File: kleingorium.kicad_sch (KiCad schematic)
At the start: 35 parts, among them J1 4017 Pins, J10 VCC, J11 GND, J12 4046 Comp In, J13 Select, J14 Input, J15 4046 SigIn, J16 4046 Comp, J17 Output, J18 4046 Comp In, J19 4046 Out, J2 4040 Output, J20 4040 Input, J21 4040 Output, J22 4017 Pins, J23 VCC, J24 GND, J3 4040 Input, J4 4046 Out, J5 4046 Comp, J6 Select, J7 Output, J8 Input, J9 4046 SigIn, Q1 2N3904, Q2 2N3904, SW1 4017 Feedback, SW2 4046 CompIn, SW3 Chain, SW4 4017 Feedback, SW5 4046 CompIn

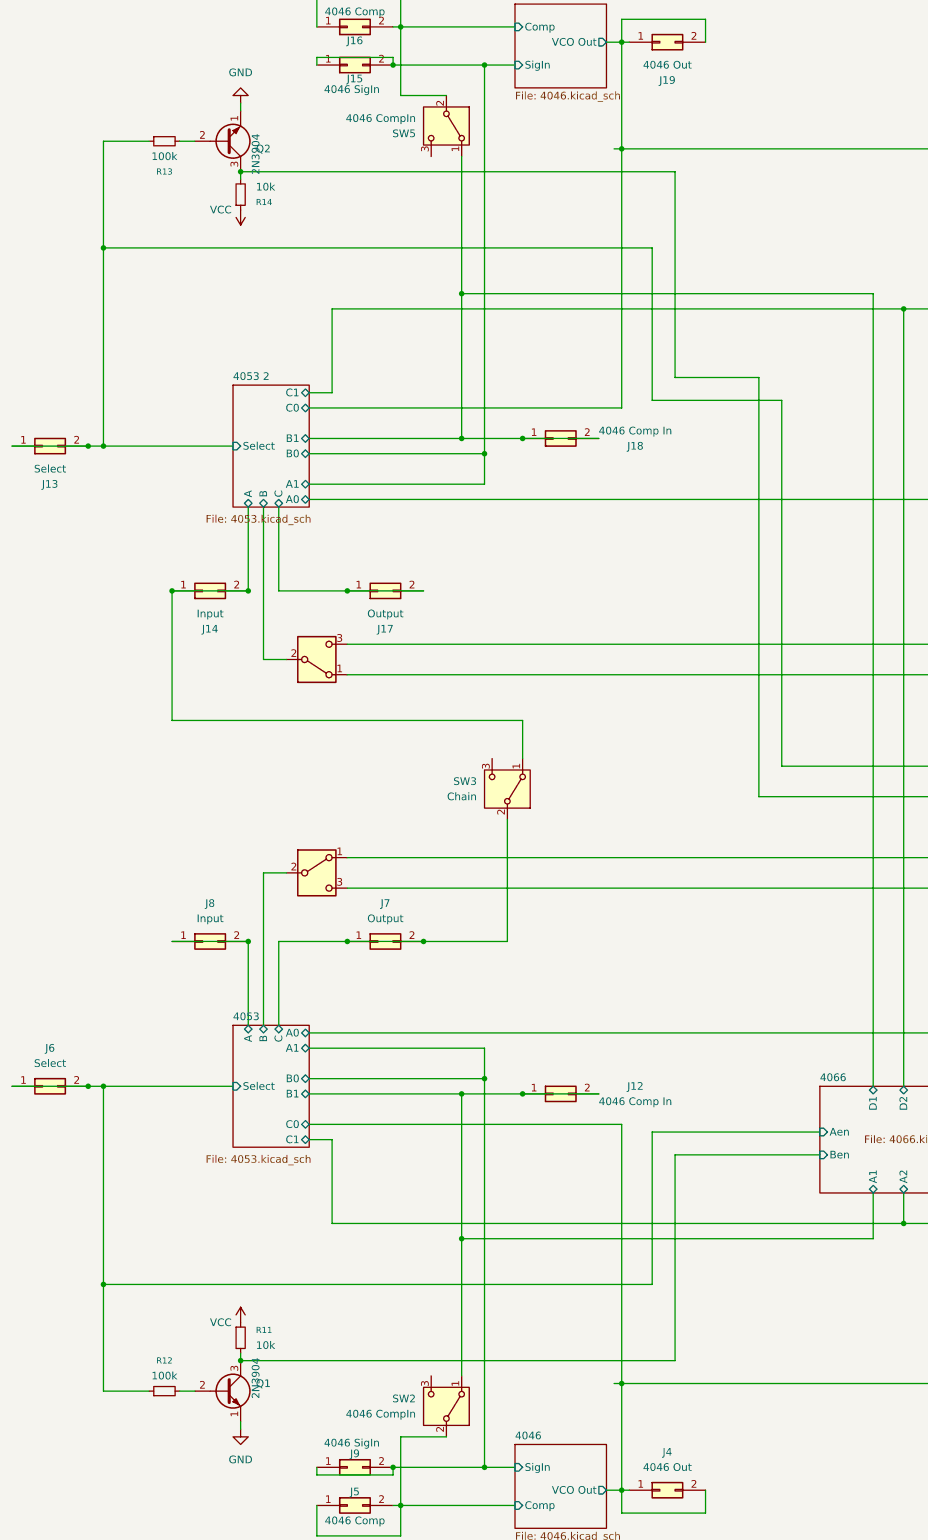
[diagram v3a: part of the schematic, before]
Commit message: fix errors with 4066 and Select
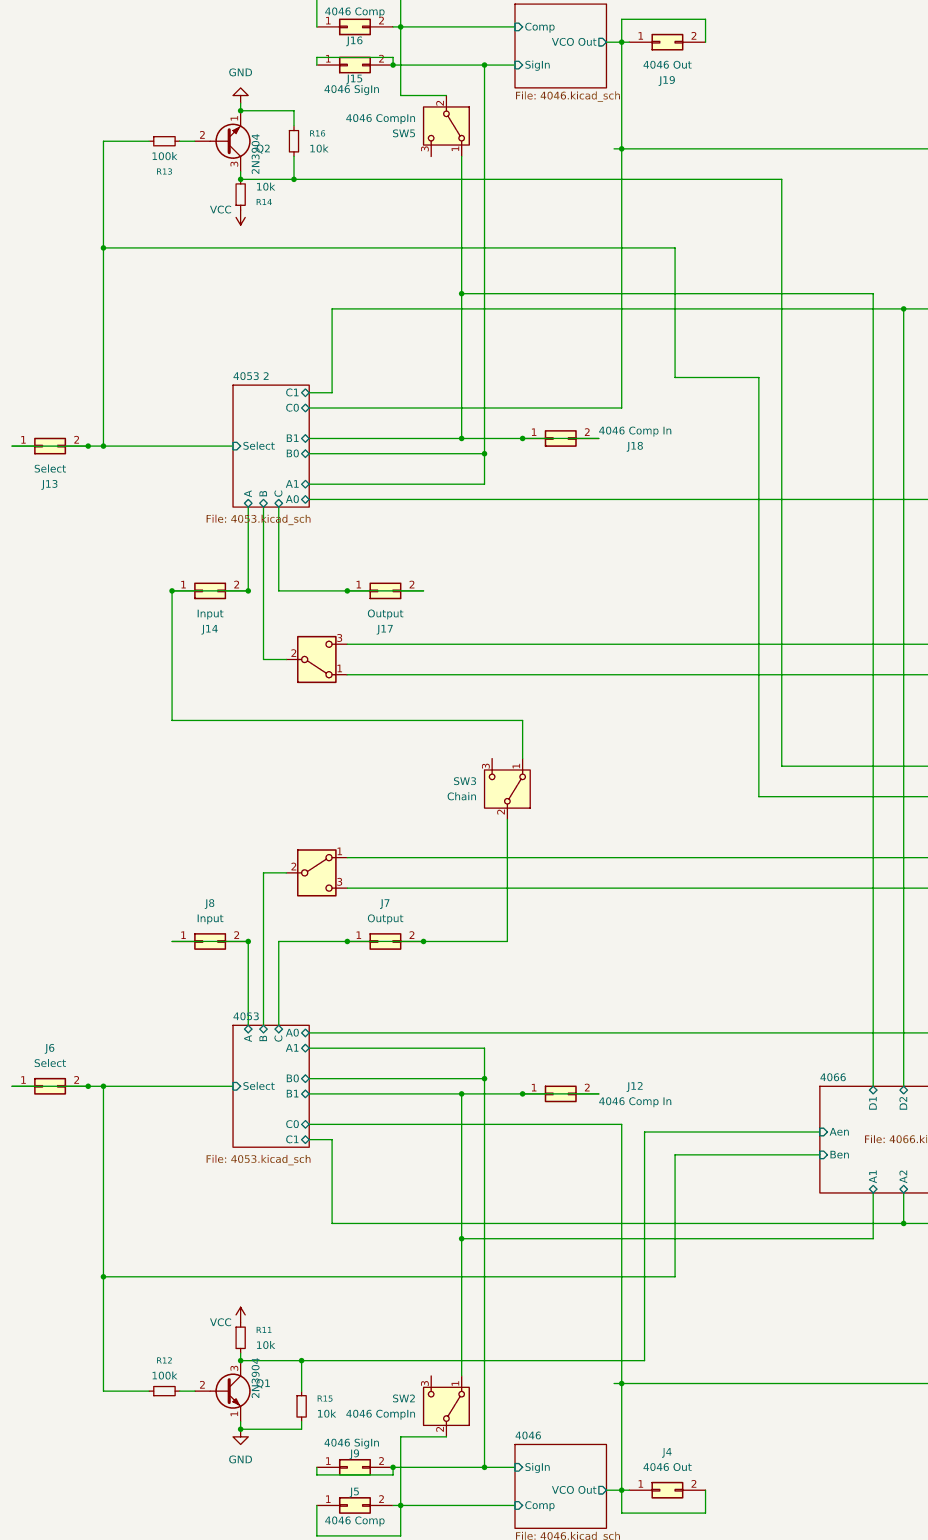
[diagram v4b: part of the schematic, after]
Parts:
- added R15, R16: 10k, Resistor_THT:R_Axial_DIN0207_L6.3mm_D2.5mm_P10.16mm_Horizontal, symbol Device:R_Small
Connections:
- net GND: now also R15.2, R16.1
- net 4066/Ben renamed 4066/Aen
- net 4066/Aen: now also R15.1
- net 4066/Cen renamed 4066/Den
- net 4066/Den: now also R16.2

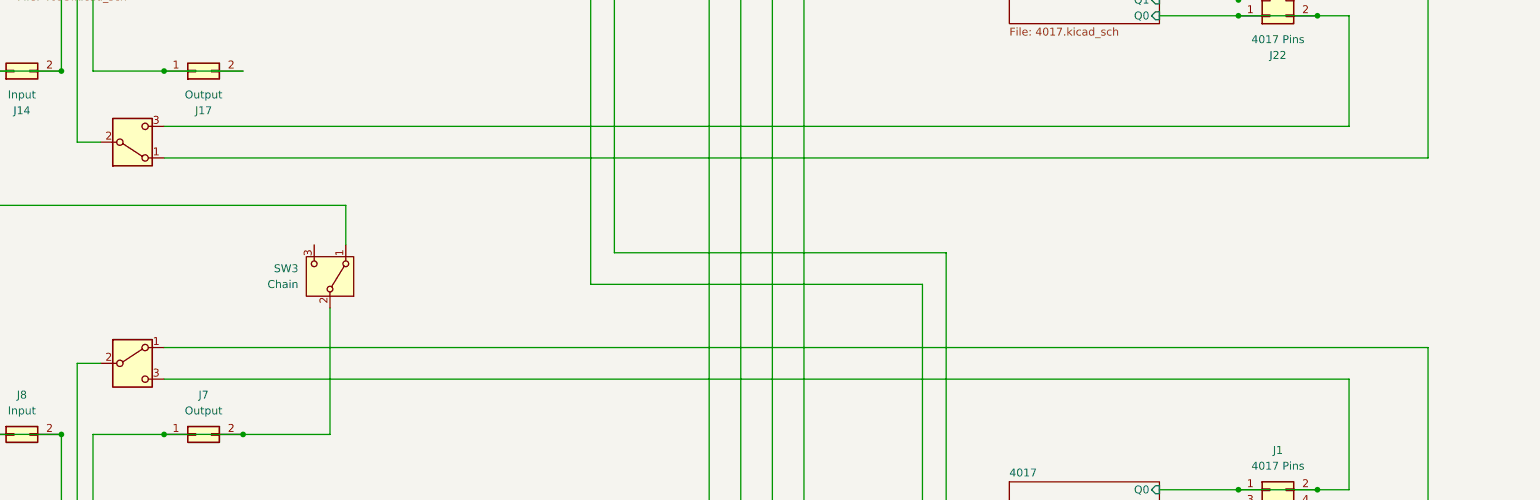
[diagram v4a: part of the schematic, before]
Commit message: change order of feedback buttons
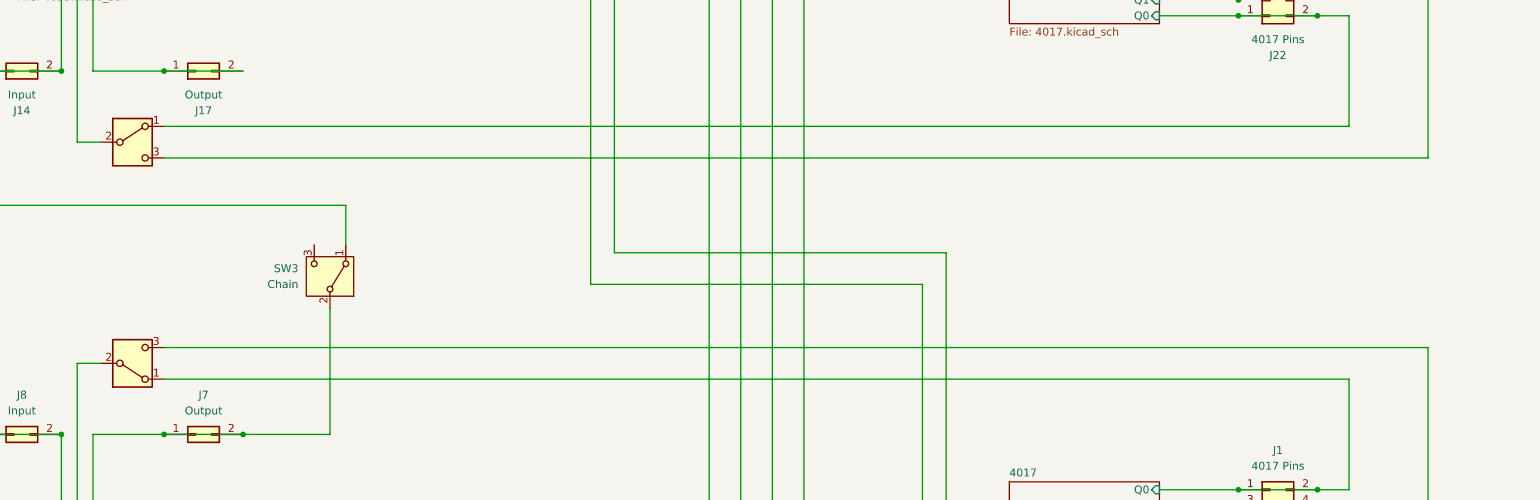
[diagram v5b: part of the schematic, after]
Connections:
- net 4017 2/Q0: now also SW4.1 (A); no longer SW4.3 (C)
- net 4017 2/Reset: now also SW4.3 (C); no longer SW4.1 (A)
- net 4017/Q0: now also SW1.1 (A); no longer SW1.3 (C)
- net 4017/Reset: now also SW1.3 (C); no longer SW1.1 (A)
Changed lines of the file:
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@@
 	(wire
 		(pts
+			(xy 294.64 161.29) (xy 294.64 212.09)
+		)
+		(stroke
+			(width 0)
+			(type default)
+		)
+	)
+	(wire
+		(pts
 			(xy 264.16 80.01) (xy 276.86 80.01)
 		)
@@
 	(wire
 		(pts
-			(xy 91.44 161.29) (xy 294.64 161.29)
-		)
-		(stroke
-			(width 0)
-			(type default)
-		)
-	)
-	(wire
-		(pts
 			(xy 251.46 90.17) (xy 264.16 90.17)
 		)
@@
 	(wire
 		(pts
+			(xy 294.64 161.29) (xy 91.44 161.29)
+		)
+		(stroke
+			(width 0)
+			(type default)
+		)
+	)
+	(wire
+		(pts
 			(xy 137.16 86.36) (xy 137.16 43.18)
 		)
@@
 	(wire
 		(pts
-			(xy 294.64 161.29) (xy 294.64 212.09)
-		)
-		(stroke
-			(width 0)
-			(type default)
-		)
-	)
-	(wire
-		(pts
 			(xy 50.8 59.69) (xy 146.05 59.69)
 		)
@@
 		(lib_id "Switch:SW_DPDT_x2")
 		(at 86.36 128.27 0)
-		(mirror x)
 		(unit 1)
 		(exclude_from_sim no)
@@
 		(on_board yes)
 		(dnp no)
-		(fields_autoplaced yes)
 		(property "Reference" "SW4"
-			(at 86.36 137.16 0)
+			(at 86.36 119.38 0)
 			(effects
 				(font
@@
 		)
 		(property "Value" "4017 Feedback"
-			(at 86.36 134.62 0)
+			(at 86.36 121.92 0)
 			(effects
 				(font
@@
 		(lib_id "Switch:SW_DPDT_x2")
 		(at 86.36 163.83 0)
+		(mirror x)
 		(unit 1)
 		(exclude_from_sim no)
@@
 		(on_board yes)
 		(dnp no)
-		(fields_autoplaced yes)
 		(property "Reference" "SW1"
-			(at 86.36 154.94 0)
+			(at 86.36 172.72 0)
 			(effects
 				(font
@@
 		)
 		(property "Value" "4017 Feedback"
-			(at 86.36 157.48 0)
+			(at 86.36 170.18 0)
 			(effects
 				(font
